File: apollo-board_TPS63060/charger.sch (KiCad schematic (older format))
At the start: 26 parts, among them J4 DNP/JST_ZH_S2B_thru, J5 DNP/JST_XH_S2B_thru, Q12 DMP2035UVT, Q15 DMN3023L, Q3 DMN3023L, Q4 2N7002A, U4 LTC4162EUFD-LAD

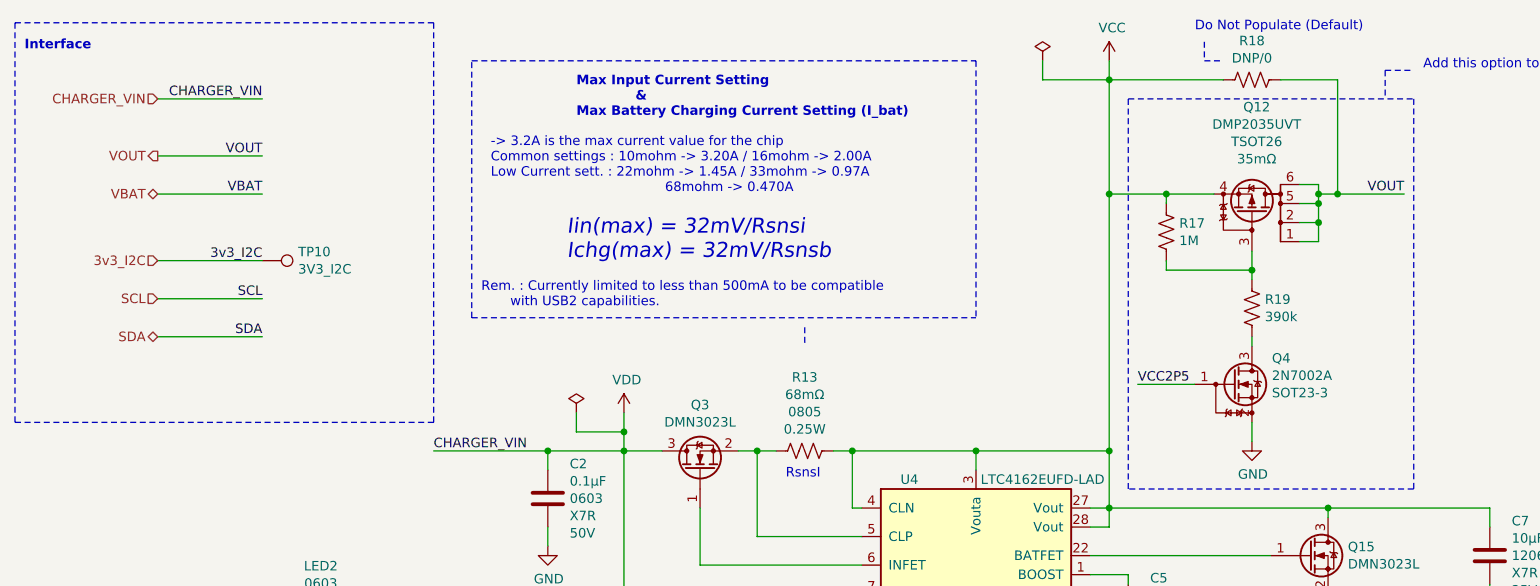
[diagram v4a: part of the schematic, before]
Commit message: Update and clean "charger" sheet + add "Vcc" test point
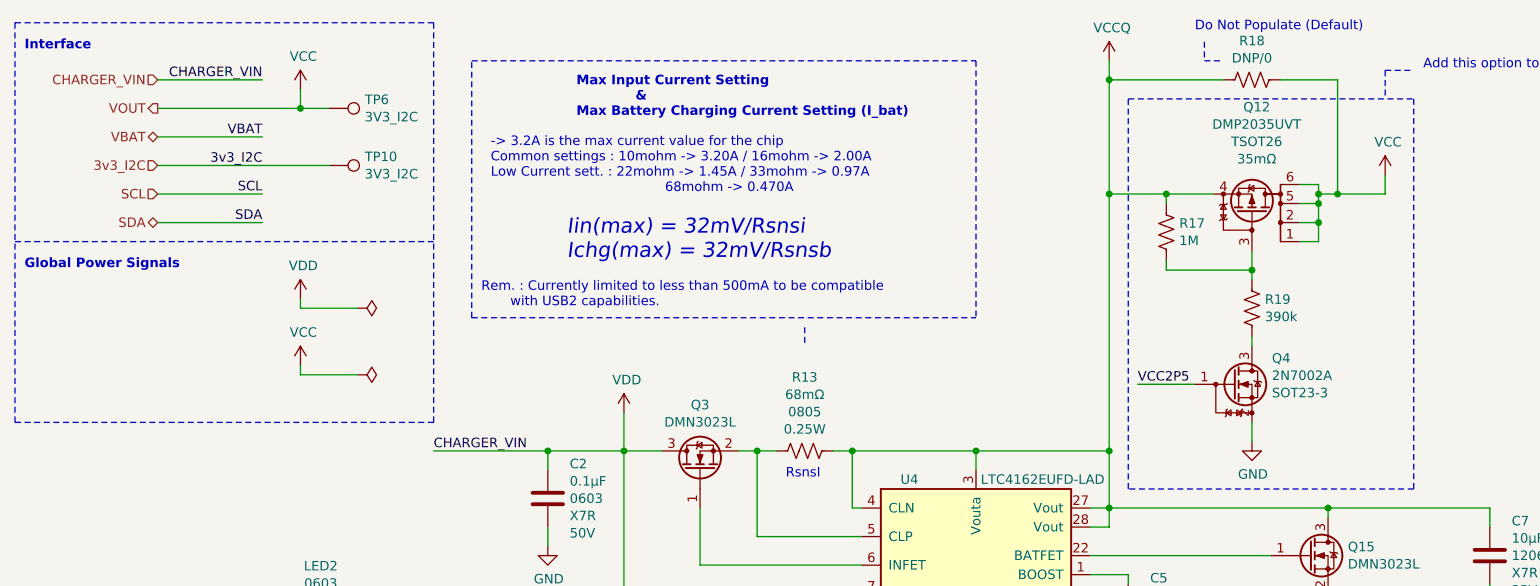
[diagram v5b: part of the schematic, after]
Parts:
- added TP6: 3V3_I2C, TestPoint:TestPoint_Pad_D1.0mm, symbol Connector:TestPoint
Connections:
- net VOUT is gone; now on net VCC: Q12.1 (D), Q12.2 (D), Q12.5 (D), Q12.6 (D), R18.1
- net VCC: now also TP6.1; no longer C7.1, Q12.4 (S), Q15.3 (D), R13.1, R17.1, R18.2, U4.27 (Vout), U4.28 (Vout), U4.3 (Vouta), U4.4 (CLN)
- new net VCCQ: C7.1, Q12.4 (S), Q15.3 (D), R13.1, R17.1, R18.2, U4.27 (Vout), U4.28 (Vout), U4.3 (Vouta), U4.4 (CLN)
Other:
- note added: "Global Power Signals"
- moved on the sheet: TP10
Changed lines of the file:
@@
 Comment4 ""
 $EndDescr
-Text HLabel 1300 1250 0    50   Output ~ 0
+Text HLabel 1300 1000 0    50   Output ~ 0
 VOUT
-Text HLabel 1300 1450 0    50   BiDi ~ 0
+Text HLabel 1300 1150 0    50   BiDi ~ 0
 VBAT
 $Comp
@@
 L power:VCC #PWR030
 U 1 1 5F745F21
-P 6300 750
-F 0 "#PWR030" H 6300 600 50  0001 C CNN
-F 1 "VCC" H 6315 923 50  0000 C CNN
-F 2 "" H 6300 750 50  0001 C CNN
-F 3 "" H 6300 750 50  0001 C CNN
-	1    6300 750
+P 7750 1350
+F 0 "#PWR030" H 7750 1200 50  0001 C CNN
+F 1 "VCC" H 7765 1523 50  0000 C CNN
+F 2 "" H 7750 1350 50  0001 C CNN
+F 3 "" H 7750 1350 50  0001 C CNN
+	1    7750 1350
 	1    0    0    -1
 $EndComp
@@
 	3750 2800 3950 2800
 Connection ~ 3750 2800
-Wire Wire Line
-	3750 2600 3750 2700
 Wire Wire Line
 	3750 2800 3750 3550
@@
 	4600 3950 5000 3950
 Wire Wire Line
-	1850 1450 1300 1450
+	1850 1150 1300 1150
 $Comp
 L power:GND #PWR035
@@
 Wire Wire Line
 	7500 850  7500 1450
-Wire Wire Line
-	1850 1250 1300 1250
 Wire Notes Line
 	6400 950  7900 950
@@
 Text Notes 1850 3900 0    50   ~ 0
 DNP : Used as an option and/or debug
-Wire Wire Line
-	5950 850  6300 850
-Wire Wire Line
-	5950 750  5950 850
-$Comp
-L power:PWR_FLAG #FLG06
-U 1 1 5F8C11C0
-P 5950 750
-F 0 "#FLG06" H 5950 825 50  0001 C CNN
-F 1 "PWR_FLAG" H 5950 923 50  0001 C CNN
-F 2 "" H 5950 750 50  0001 C CNN
-F 3 "~" H 5950 750 50  0001 C CNN
-	1    5950 750
-	1    0    0    -1
-$EndComp
-Wire Wire Line
-	3500 2700 3750 2700
-Wire Wire Line
-	3500 2600 3500 2700
-$Comp
-L power:PWR_FLAG #FLG05
-U 1 1 5FC883D2
-P 3500 2600
-F 0 "#FLG05" H 3500 2675 50  0001 C CNN
-F 1 "PWR_FLAG" H 3500 2773 50  0001 C CNN
-F 2 "" H 3500 2600 50  0001 C CNN
-F 3 "~" H 3500 2600 50  0001 C CNN
-	1    3500 2600
-	1    0    0    -1
-$EndComp
-Connection ~ 3750 2700
-Wire Wire Line
-	3750 2700 3750 2800
 $Comp
 L Device:R_US R14
@@
 Wire Wire Line
 	5300 5550 5300 5500
-Text HLabel 1300 950  0    50   Input ~ 0
+Text HLabel 1300 850  0    50   Input ~ 0
 CHARGER_VIN
-Text Label 1850 950  2    50   ~ 0
+Text Label 1850 850  2    50   ~ 0
 CHARGER_VIN
 Wire Wire Line
-	1850 950  1300 950
+	1850 850  1300 850
 Text Notes 1400 5450 0    50   ~ 0
 See Table 5 in the datasheet
-Text HLabel 1300 1800 0    50   Input ~ 0
+Text HLabel 1300 1300 0    50   Input ~ 0
 3v3_I2C
 Wire Wire Line
-	1300 1800 1850 1800
-Text Label 1850 1800 2    50   ~ 0
+	1300 1300 2200 1300
+Text Label 1850 1300 2    50   ~ 0
 3v3_I2C
 Text Label 4600 3850 0    50   ~ 0
@@
 Wire Wire Line
 	4600 3850 5000 3850
-Text Label 7850 1450 2    50   ~ 0
-VOUT
-Wire Wire Line
-	7850 1450 7500 1450
 Connection ~ 7500 1450
-Text Label 1850 1250 2    50   ~ 0
-VOUT
 Text Label 8150 4350 2    50   ~ 0
 VBAT
-Text HLabel 1300 2000 0    50   Input ~ 0
+Text HLabel 1300 1450 0    50   Input ~ 0
 SCL
-Text HLabel 1300 2200 0    50   BiDi ~ 0
+Text HLabel 1300 1600 0    50   BiDi ~ 0
 SDA
 Wire Wire Line
-	1300 2200 1850 2200
-Wire Wire Line
-	1300 2000 1850 2000
+	1300 1600 1850 1600
+Wire Wire Line
+	1300 1450 1850 1450
+Text Label 1850 1150 2    50   ~ 0
+VBAT
 Text Label 1850 1450 2    50   ~ 0
-VBAT
-Text Label 1850 2000 2    50   ~ 0
 SCL
-Text Label 1850 2200 2    50   ~ 0
+Text Label 1850 1600 2    50   ~ 0
 SDA
 Text Label 4600 3950 0    50   ~ 0
@@
 $EndComp
 Wire Notes Line
-	550  2650 2750 2650
+	550  1700 2750 1700
 Wire Notes Line
 	550  550  2750 550
@@
 L Connector:TestPoint TP10
 U 1 1 5FD9160B
-P 1850 1800
-F 0 "TP10" V 1804 1988 50  0000 L CNN
-F 1 "3V3_I2C" V 1895 1988 50  0000 L CNN
-F 2 "TestPoint:TestPoint_Pad_D1.0mm" H 2050 1800 50  0001 C CNN
-F 3 "~" H 2050 1800 50  0001 C CNN
-	1    1850 1800
+P 2200 1300
+F 0 "TP10" V 2154 1488 50  0000 L CNN
+F 1 "3V3_I2C" V 2245 1488 50  0000 L CNN
+F 2 "TestPoint:TestPoint_Pad_D1.0mm" H 2400 1300 50  0001 C CNN
+F 3 "~" H 2400 1300 50  0001 C CNN
+	1    2200 1300
 	0    1    1    0
 $EndComp
@@
 	1    0    0    -1
 $EndComp
+$Comp
+L power:VCCQ #PWR013
+U 1 1 60FDB38C
+P 6300 750
+F 0 "#PWR013" H 6300 600 50  0001 C CNN
+F 1 "VCCQ" H 6315 923 50  0000 C CNN
+F 2 "" H 6300 750 50  0001 C CNN
+F 3 "" H 6300 750 50  0001 C CNN
+	1    6300 750
+	1    0    0    -1
+$EndComp
+Text Notes 600  1850 0    50   ~ 10
+Global Power Signals
+$Comp
+L power:VDD #PWR010
+U 1 1 61009CFF
+P 2050 2000
+F 0 "#PWR010" H 2050 1850 50  0001 C CNN
+F 1 "VDD" H 2065 2173 50  0000 C CNN
+F 2 "" H 2050 2000 50  0001 C CNN
+F 3 "" H 2050 2000 50  0001 C CNN
+	1    2050 2000
+	1    0    0    -1
+$EndComp
+$Comp
+L power:PWR_FLAG #FLG01
+U 1 1 6100A2B8
+P 2350 2050
+F 0 "#FLG01" H 2350 2125 50  0001 C CNN
+F 1 "PWR_FLAG" H 2350 2223 50  0001 C CNN
+F 2 "" H 2350 2050 50  0001 C CNN
+F 3 "~" H 2350 2050 50  0001 C CNN
+	1    2350 2050
+	0    1    1    0
+$EndComp
+Wire Wire Line
+	3750 2600 3750 2800
+Wire Wire Line
+	2050 2000 2050 2050
+Wire Wire Line
+	2050 2050 2350 2050
+$Comp
+L power:PWR_FLAG #FLG06
+U 1 1 5F8C11C0
+P 2350 2400
+F 0 "#FLG06" H 2350 2475 50  0001 C CNN
+F 1 "PWR_FLAG" H 2350 2573 50  0001 C CNN
+F 2 "" H 2350 2400 50  0001 C CNN
+F 3 "~" H 2350 2400 50  0001 C CNN
+	1    2350 2400
+	0    1    1    0
+$EndComp
+$Comp
+L power:VCC #PWR011
+U 1 1 6103092B
+P 2050 2350
+F 0 "#PWR011" H 2050 2200 50  0001 C CNN
+F 1 "VCC" H 2065 2523 50  0000 C CNN
+F 2 "" H 2050 2350 50  0001 C CNN
+F 3 "" H 2050 2350 50  0001 C CNN
+	1    2050 2350
+	1    0    0    -1
+$EndComp
+Wire Wire Line
+	2050 2350 2050 2400
+Wire Wire Line
+	2050 2400 2350 2400
+Wire Wire Line
+	7750 1450 7500 1450
+Wire Wire Line
+	7750 1450 7750 1350
+Wire Notes Line
+	550  2650 2750 2650
+$Comp
+L power:VCC #PWR07
+U 1 1 6105FA1F
+P 2050 900
+F 0 "#PWR07" H 2050 750 50  0001 C CNN
+F 1 "VCC" H 2065 1073 50  0000 C CNN
+F 2 "" H 2050 900 50  0001 C CNN
+F 3 "" H 2050 900 50  0001 C CNN
+	1    2050 900
+	1    0    0    -1
+$EndComp
+Wire Wire Line
+	2050 1000 2050 900
+Wire Wire Line
+	1300 1000 2050 1000
+$Comp
+L Connector:TestPoint TP6
+U 1 1 61067853
+P 2200 1000
+F 0 "TP6" V 2154 1188 50  0000 L CNN
+F 1 "3V3_I2C" V 2245 1188 50  0000 L CNN
+F 2 "TestPoint:TestPoint_Pad_D1.0mm" H 2400 1000 50  0001 C CNN
+F 3 "~" H 2400 1000 50  0001 C CNN
+	1    2200 1000
+	0    1    1    0
+$EndComp
+Wire Wire Line
+	2200 1000 2050 1000
+Connection ~ 2050 1000
 $EndSCHEMATC

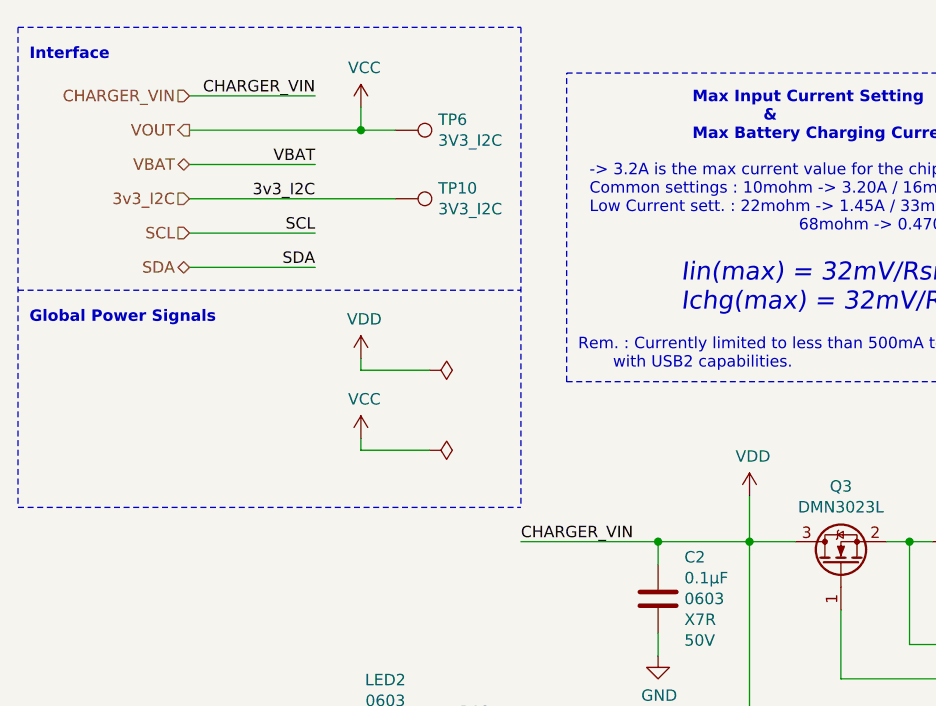
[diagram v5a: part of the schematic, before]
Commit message: Rename some power signal on Schematic to improve readability.
+ Misc. updates
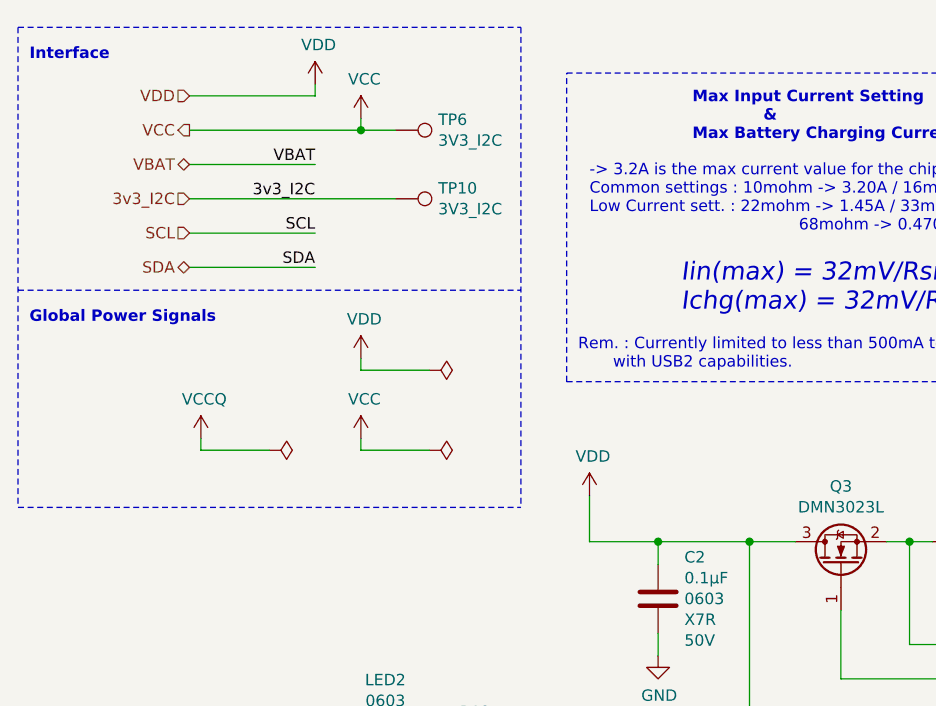
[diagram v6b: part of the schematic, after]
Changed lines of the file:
@@
 $EndDescr
 Text HLabel 1300 1000 0    50   Output ~ 0
-VOUT
+VCC
 Text HLabel 1300 1150 0    50   BiDi ~ 0
 VBAT
@@
 F 3 "" H 5800 5600 50  0001 C CNN
 	1    5800 5600
-	1    0    0    -1
-$EndComp
-$Comp
-L power:VDD #PWR025
-U 1 1 5F7457C8
-P 3750 2600
-F 0 "#PWR025" H 3750 2450 50  0001 C CNN
-F 1 "VDD" H 3765 2773 50  0000 C CNN
-F 2 "" H 3750 2600 50  0001 C CNN
-F 3 "" H 3750 2600 50  0001 C CNN
-	1    3750 2600
 	1    0    0    -1
 $EndComp
@@
 	6300 1450 6300 2800
 Connection ~ 6300 850
-Text Label 2750 2800 0    50   ~ 0
-CHARGER_VIN
-Wire Wire Line
-	2750 2800 3350 2800
+Wire Wire Line
+	3050 2800 3350 2800
 Connection ~ 3350 2800
 Wire Wire Line
@@
 	5300 5550 5300 5500
 Text HLabel 1300 850  0    50   Input ~ 0
-CHARGER_VIN
-Text Label 1850 850  2    50   ~ 0
-CHARGER_VIN
+VDD
 Wire Wire Line
 	1850 850  1300 850
@@
 $EndComp
 Wire Wire Line
-	3750 2600 3750 2800
-Wire Wire Line
 	2050 2000 2050 2050
 Wire Wire Line
@@
 L power:VCC #PWR07
 U 1 1 6105FA1F
-P 2050 900
-F 0 "#PWR07" H 2050 750 50  0001 C CNN
-F 1 "VCC" H 2065 1073 50  0000 C CNN
-F 2 "" H 2050 900 50  0001 C CNN
-F 3 "" H 2050 900 50  0001 C CNN
-	1    2050 900
-	1    0    0    -1
-$EndComp
-Wire Wire Line
-	2050 1000 2050 900
+P 2050 950
+F 0 "#PWR07" H 2050 800 50  0001 C CNN
+F 1 "VCC" H 2065 1123 50  0000 C CNN
+F 2 "" H 2050 950 50  0001 C CNN
+F 3 "" H 2050 950 50  0001 C CNN
+	1    2050 950
+	1    0    0    -1
+$EndComp
+Wire Wire Line
+	2050 1000 2050 950
 Wire Wire Line
 	1300 1000 2050 1000
@@
 	2200 1000 2050 1000
 Connection ~ 2050 1000
+$Comp
+L power:VDD #PWR0117
+U 1 1 610A4A6D
+P 1850 800
+F 0 "#PWR0117" H 1850 650 50  0001 C CNN
+F 1 "VDD" H 1865 973 50  0000 C CNN
+F 2 "" H 1850 800 50  0001 C CNN
+F 3 "" H 1850 800 50  0001 C CNN
+	1    1850 800
+	1    0    0    -1
+$EndComp
+$Comp
+L power:VDD #PWR025
+U 1 1 5F7457C8
+P 3050 2600
+F 0 "#PWR025" H 3050 2450 50  0001 C CNN
+F 1 "VDD" H 3065 2773 50  0000 C CNN
+F 2 "" H 3050 2600 50  0001 C CNN
+F 3 "" H 3050 2600 50  0001 C CNN
+	1    3050 2600
+	1    0    0    -1
+$EndComp
+Wire Wire Line
+	3050 2600 3050 2800
+Wire Wire Line
+	1850 800  1850 850
+$Comp
+L power:PWR_FLAG #FLG0107
+U 1 1 610DBC23
+P 1650 2400
+F 0 "#FLG0107" H 1650 2475 50  0001 C CNN
+F 1 "PWR_FLAG" H 1650 2573 50  0001 C CNN
+F 2 "" H 1650 2400 50  0001 C CNN
+F 3 "~" H 1650 2400 50  0001 C CNN
+	1    1650 2400
+	0    1    1    0
+$EndComp
+Wire Wire Line
+	1350 2350 1350 2400
+Wire Wire Line
+	1350 2400 1650 2400
+$Comp
+L power:VCCQ #PWR0118
+U 1 1 610E2466
+P 1350 2350
+F 0 "#PWR0118" H 1350 2200 50  0001 C CNN
+F 1 "VCCQ" H 1365 2523 50  0000 C CNN
+F 2 "" H 1350 2350 50  0001 C CNN
+F 3 "" H 1350 2350 50  0001 C CNN
+	1    1350 2350
+	1    0    0    -1
+$EndComp
 $EndSCHEMATC

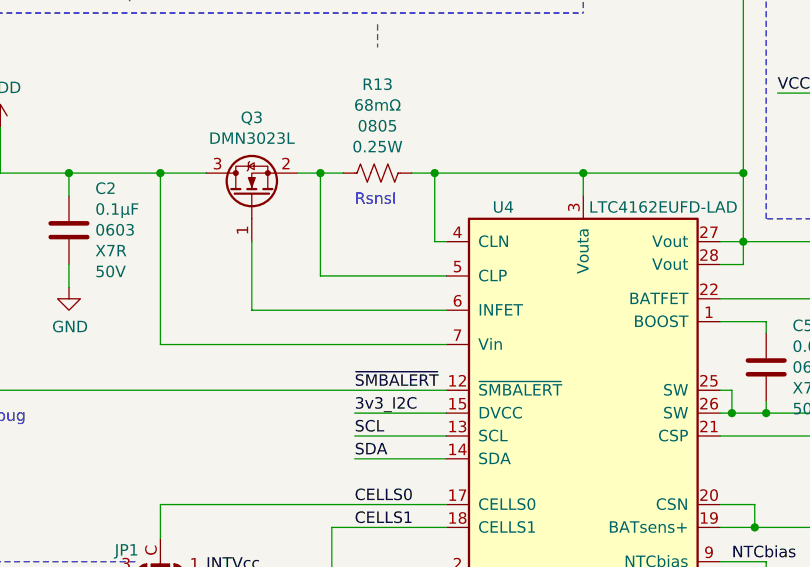
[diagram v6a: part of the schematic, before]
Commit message: Improve Tracks width and Vias around LTC4162-L (Q3)
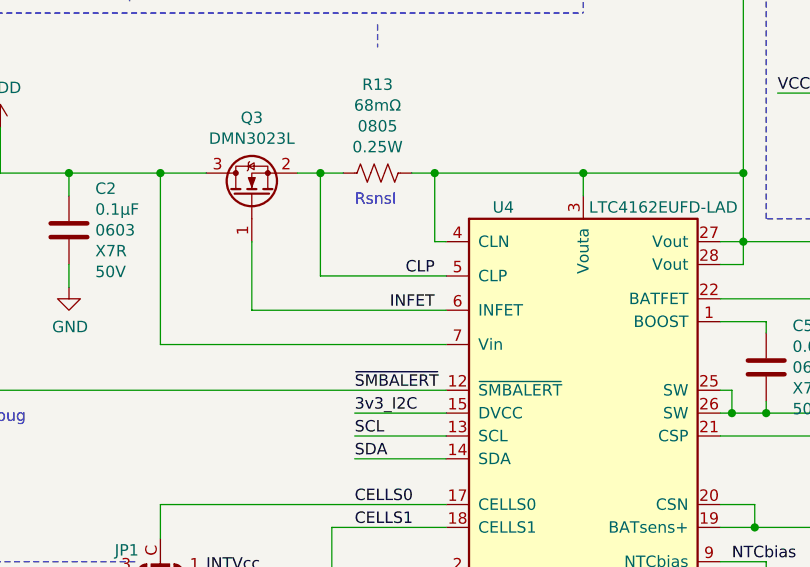
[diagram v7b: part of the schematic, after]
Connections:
- net CLP: now reaches Q3.2 (S), R13.2, U4.5 (CLP)
- net INFET: now reaches Q3.1 (G), U4.6 (INFET)
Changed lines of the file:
@@
 	1    0    0    -1
 $EndComp
+Text Label 4950 3250 2    50   ~ 0
+CLP
+Text Label 4950 3400 2    50   ~ 0
+INFET
 $EndSCHEMATC

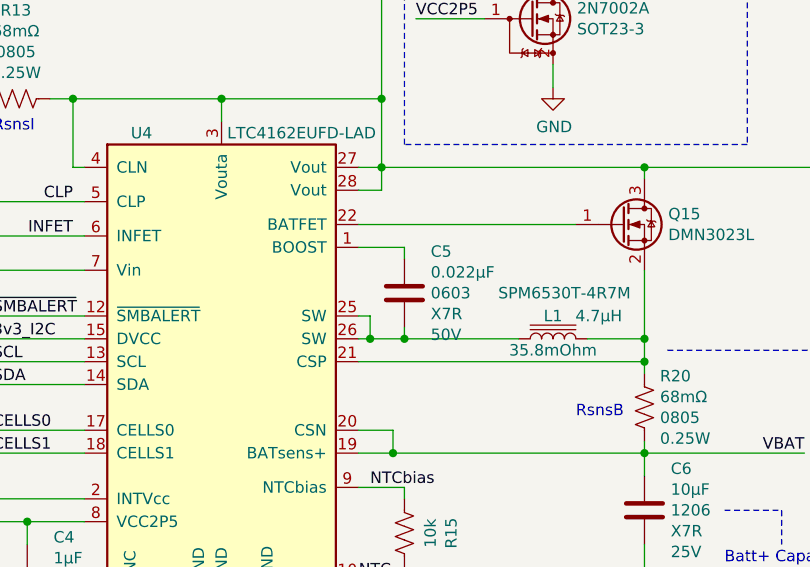
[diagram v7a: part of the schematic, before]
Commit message: Q15 Track width issue correction
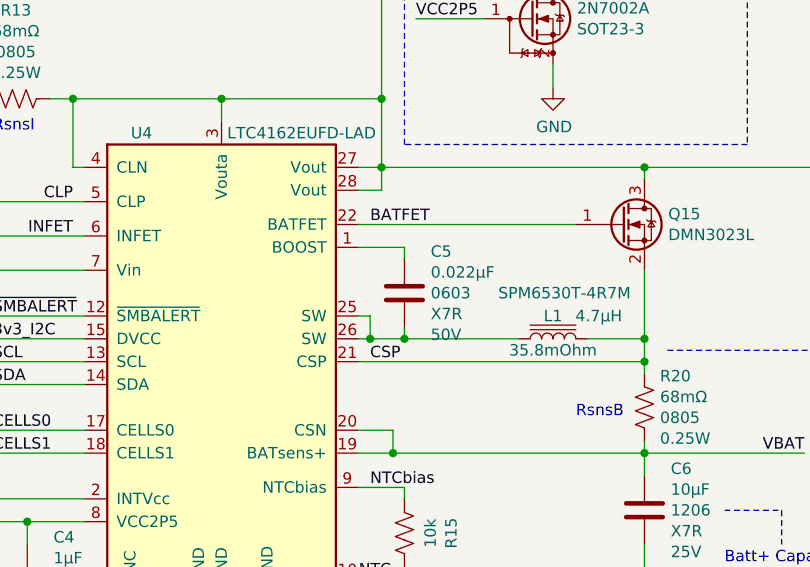
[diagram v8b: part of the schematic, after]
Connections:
- net CSP: now reaches L1.2, Q15.2 (S), R20.2, U4.21 (CSP)
- net BATFET: now reaches Q15.1 (G), U4.22 (BATFET)
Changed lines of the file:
@@
 Text Label 4950 3400 2    50   ~ 0
 INFET
+Text Label 6250 3950 0    50   ~ 0
+CSP
+Text Label 6250 3350 0    50   ~ 0
+BATFET
 $EndSCHEMATC
